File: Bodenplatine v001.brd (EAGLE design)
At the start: 160 x 100 mm, 0 parts

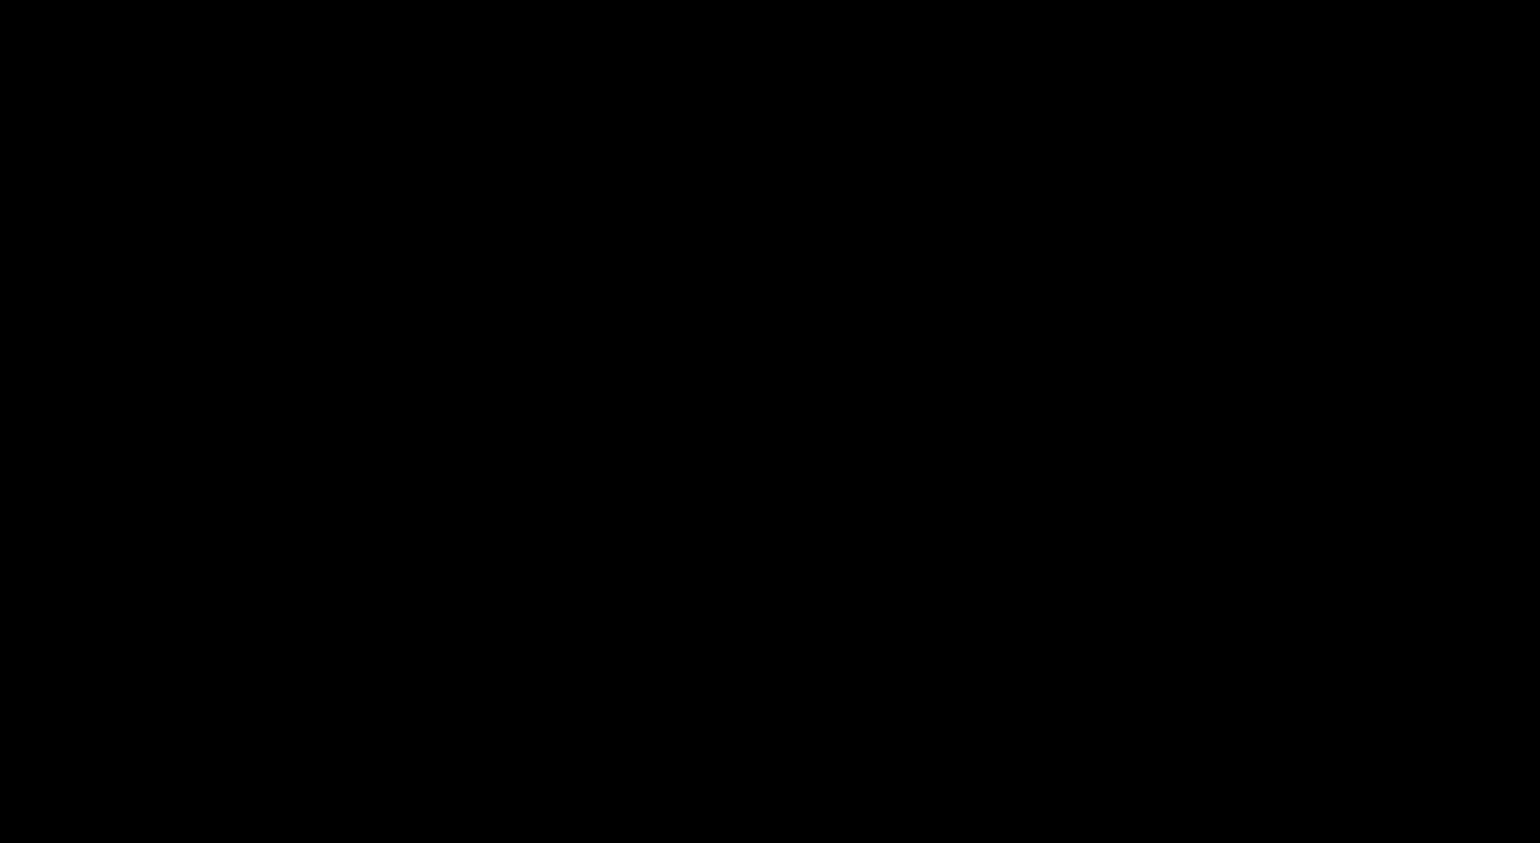
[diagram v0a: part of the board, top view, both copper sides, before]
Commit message: Erste Version der Projekt eigenen Eagle Library
Alle Parts sollen von nun an für jedes Projekt in eine seperate Eagle lbr Datei gepackt werden. Nur Teile aus dieser Library sollen verwendet werden.

Das geschieht um einen besseren Überblick über die verwendeten Teile zu erhalten. Außerdem kann die Eagle Zeichnung incl. der Parts weiter gegeben werden.
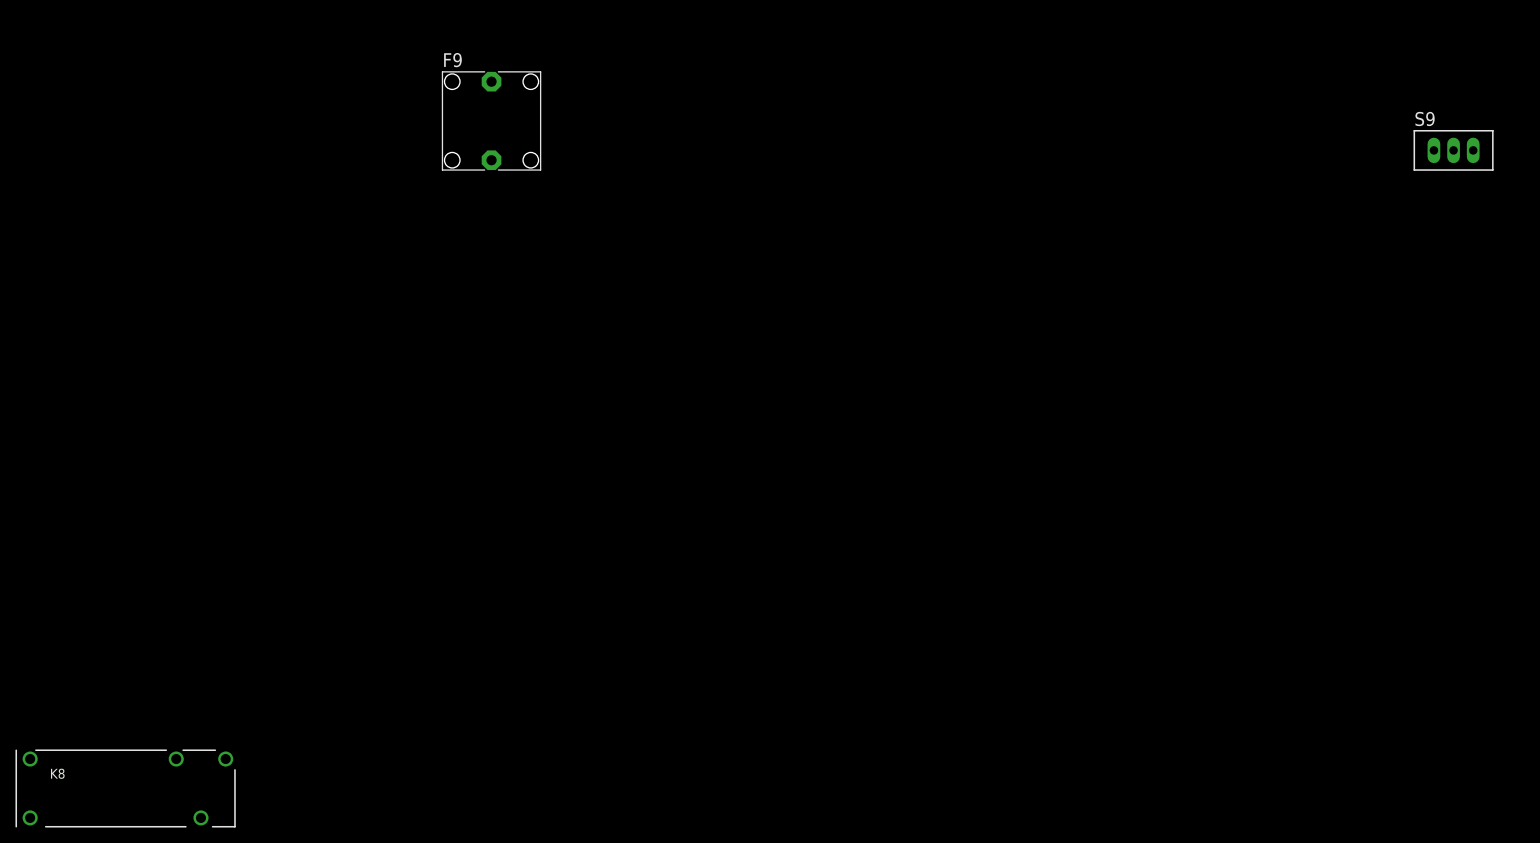
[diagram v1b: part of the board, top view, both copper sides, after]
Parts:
- added F9: (no value), xMZ-Mod-Touch-Bodenplatine:F456
- added K8: RY210005, xMZ-Mod-Touch-Bodenplatine:RY-II
- added S9: TL39PO, xMZ-Mod-Touch-Bodenplatine:TL3XPO
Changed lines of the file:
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@@
 </autorouter>
 <elements>
+<element name="S9" library="xMZ-Mod-Touch-Bodenplatine" package="TL3XPO" value="TL39PO" x="-97.79" y="6.35"/>
+<element name="F9" library="xMZ-Mod-Touch-Bodenplatine" package="F456" value="" x="-222.25" y="10.16">
+<attribute name="OC_NEWARK" value="unknown" x="-222.25" y="10.16" size="1.778" layer="27" font="vector" ratio="15" display="off"/>
+<attribute name="MPN" value="" x="-222.25" y="10.16" size="1.778" layer="27" font="vector" ratio="15" display="off"/>
+<attribute name="MF" value="" x="-222.25" y="10.16" size="1.778" layer="27" font="vector" ratio="15" display="off"/>
+<attribute name="OC_FARNELL" value="unknown" x="-222.25" y="10.16" size="1.778" layer="27" font="vector" ratio="15" display="off"/>
+</element>
+<element name="K8" library="xMZ-Mod-Touch-Bodenplatine" package="RY-II" value="RY210005" x="-269.24" y="-76.2">
+<attribute name="OC_NEWARK" value="08H3762" x="-269.24" y="-76.2" size="1.778" layer="27" font="vector" ratio="15" display="off"/>
+<attribute name="MPN" value="RY210005" x="-269.24" y="-76.2" size="1.778" layer="27" font="vector" ratio="15" display="off"/>
+<attribute name="MF" value="TYCO ELECTRONICS" x="-269.24" y="-76.2" size="1.778" layer="27" font="vector" ratio="15" display="off"/>
+<attribute name="OC_FARNELL" value="unknown" x="-269.24" y="-76.2" size="1.778" layer="27" font="vector" ratio="15" display="off"/>
+</element>
 </elements>
 <signals>

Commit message: Erste fast fertige Version des Schaltplans der Bodebplatine
Es fehlt nur noch die Wago Klemme für L/N/PE Netzteil und 12V+/-
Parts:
- removed S9: TL39PO, xMZ-Mod-Touch-Bodenplatine:TL3XPO
- added D1, D13, D14, D15, D16, D2, D25, D3, D4: BAT54, diode:SOT23
- added D10, D11, D12, D21, D22, D23, D24, D27, D9: 1N4148W, diode:DO35-7
- added D17, D18, D19, D20, D26, D5, D6, D7, D8: Yellow, SparkFun-LED:LED-0603
- added F1, F10, F11, F12, F2, F3, F4, F5, F6, F7, F8: (no value), xMZ-Mod-Touch-Bodenplatine:F456
- added JP1: (no value), pinhead:2X10
- added K1, K2, K3, K4, K5, K6, K7, K9: RY612012, xMZ-Mod-Touch-Bodenplatine:RY-II
- added Q1, Q2, Q3, Q4, Q5, Q6, Q7, Q8, Q9: BC846, AWJLEagleLib:SOT-363
- added R1, R13, R14, R15, R16, R2, R25, R3, R4: 270R, rcl:M0805
- added R10, R11, R12, R21, R22, R23, R24, R27, R9: 10k, rcl:R0603
- added R17, R18, R19, R20, R26, R5, R6, R7, R8: 2k2, rcl:R0603
- added X1, X13, X2, X3, X4, X5, X6, X7, X8, X9: SPRINGCON_AST125_5X2, xMZ-Mod-Touch-Bodenplatine:SPRINGCON_AST125_5X2
- added X10: SPRINGCON_AST125_3X2, xMZ-Mod-Touch-Bodenplatine:SPRINGCON_AST125_3X2
- added X11, X12: SPRINGCON_AST125_4X2, xMZ-Mod-Touch-Bodenplatine:SPRINGCON_AST125_4X2
- K8: value RY210005 -> RY612012
- moved K8 765.8 mm to (-882.6, -534.7)
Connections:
- new net 12V: F10.1, F11.1, JP1.12
- new net 5V: JP1.10, JP1.9
- new net A-: JP1.20, X13.4, X13.4'
- new net AKKU: JP1.16
- new net B+: JP1.19, X13.3
- new net GND: D17.C, D18.C, D19.C, D20.C, D26.C, D5.C, D6.C, D7.C, D8.C, JP1.7, JP1.8, Q1.1, Q2.1, Q3.1, Q4.1, Q5.1, Q6.1, Q7.1, Q8.1, Q9.1, X13.2
- new net L: F9.1
- new net N: X1.4, X2.4, X3.4, X4.4, X5.4, X6.4, X7.4, X8.4, X9.4
- new net N$1: F1.1, X1.2
- new net N$10: Q1.2, R9.2
- new net N$108: JP1.17
- new net N$11: D9.C, K1.A2
- new net N$12: F2.2, K2.11
- new net N$13: D2.1, R2.1
- new net N$14: D2.3, R10.1, R6.2
- new net N$15: D6.A, R6.1
- new net N$16: Q2.2, R10.2
- new net N$17: D10.C, K2.A2
- new net N$18: D10.A, K2.A1, Q2.6
- new net N$19: F2.1, X2.2
- new net N$2: K1.14, X1.3
- new net N$20: K2.12, X2.1
- new net N$21: K3.14, X3.3
- new net N$22: F3.2, K3.11
- new net N$23: D3.1, R3.1
- new net N$24: D3.3, R11.1, R7.2
- new net N$25: D7.A, R7.1
- new net N$26: Q3.2, R11.2
- new net N$27: D11.C, K3.A2
- new net N$28: D11.A, K3.A1, Q3.6
- new net N$29: F3.1, X3.2
- new net N$3: F1.2, K1.11
- new net N$30: K3.12, X3.1
- new net N$31: K4.14, X4.3
- new net N$32: F4.2, K4.11
- new net N$33: D4.1, R4.1
- new net N$34: D4.3, R12.1, R8.2
- new net N$35: D8.A, R8.1
- new net N$36: Q4.2, R12.2
- new net N$37: D12.C, K4.A2
- new net N$38: D12.A, K4.A1, Q4.6
- new net N$39: F4.1, X4.2
- new net N$4: K1.12, X1.1
- new net N$40: K4.12, X4.1
- new net N$41: K5.14, X5.3
- new net N$42: F5.2, K5.11
- new net N$43: D13.1, R13.1
- new net N$44: D13.3, R17.2, R21.1
- new net N$45: D17.A, R17.1
- new net N$46: Q5.2, R21.2
- new net N$47: D21.C, K5.A2
- new net N$48: D21.A, K5.A1, Q5.6
- new net N$49: F5.1, X5.2
- new net N$5: D9.A, K1.A1, Q1.6
- new net N$50: K5.12, X5.1
- new net N$51: K6.14, X6.3
- new net N$52: F6.2, K6.11
- new net N$53: D14.1, R14.1
- new net N$54: D14.3, R18.2, R22.1
- new net N$55: D18.A, R18.1
- new net N$56: Q6.2, R22.2
- new net N$57: D22.C, K6.A2
- new net N$58: D22.A, K6.A1, Q6.6
- new net N$59: F6.1, X6.2
- new net N$6: K2.14, X2.3
- new net N$60: K6.12, X6.1
- new net N$61: K7.14, X7.3
- new net N$62: F7.2, K7.11
- new net N$63: D15.1, R15.1
- new net N$64: D15.3, R19.2, R23.1
- new net N$65: D19.A, R19.1
- new net N$66: Q7.2, R23.2
- new net N$67: D23.C, K7.A2
- new net N$68: D23.A, K7.A1, Q7.6
- new net N$69: F7.1, X7.2
- new net N$7: D1.1, R1.1
- new net N$70: K7.12, X7.1
- new net N$71: K8.14, X8.3
- new net N$72: F8.2, K8.11
- new net N$73: D16.1, R16.1
- new net N$74: D16.3, R20.2, R24.1
- new net N$75: D20.A, R20.1
- new net N$76: Q8.2, R24.2
- new net N$77: D24.C, K8.A2
- new net N$78: D24.A, K8.A1, Q8.6
- new net N$79: F8.1, X8.2
- new net N$8: D1.3, R5.2, R9.1
- new net N$80: K8.12, X8.1
- new net N$81: K9.14, X9.3
- new net N$82: F12.2, K9.11
- new net N$83: D25.1, R25.1
- new net N$84: D25.3, R26.2, R27.1
- new net N$85: D26.A, R26.1
- new net N$86: Q9.2, R27.2
- new net N$87: D27.C, K9.A2
- new net N$88: D27.A, K9.A1, Q9.6
- new net N$89: F12.1, X9.2
- new net N$9: D5.A, R5.1
- new net N$90: K9.12, X9.1
- new net N$91: F9.2
- new net N$92: F11.2, X13.1
- new net N$94: F10.2
- new net N$98: JP1.18
- new net P1: JP1.6, R25.2
- new net P2: JP1.4, R1.2
- new net P3: JP1.2, R2.2
- new net P4: JP1.1, R3.2
- new net P5: JP1.3, R4.2
- new net P6: JP1.5, R13.2
- new net P7: JP1.11, R14.2
- new net P8: JP1.13, R15.2
- new net P9: JP1.15, R16.2
- new net PE: X1.5, X1.5', X2.5, X2.5', X3.5, X3.5', X4.5, X4.5', X5.5, X5.5', X6.5, X6.5', X7.5, X7.5', X8.5, X8.5', X9.5, X9.5'
- new net SCHIRM: X13.5
- new net UB: JP1.14

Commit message: Begin mit dem Bord der Bodenplatine
Schriften in den Schaltplänen einheitlich gemacht (Layer und Große)
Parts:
- added H1, H2, H3, H4: MOUNT-HOLE3.3, holes:3,3
- added X14: 236-403, con-wago_236:P-236-403
- added X15: 236-402, con-wago_236:P-236-402
- F1, F11, F12, F2, F3, F4, F5, F6, F7, F8: value (none) -> 3,15AT
- F10: value (none) -> 6,3AT
- F9: value (none) -> 10AT
- JP1: value (none) -> Stiftleiste 2x20 pol
- moved X13 1066.3 mm to (25.7, -194.4)
- moved X2 980.6 mm to (-53.9, 124.8)
- moved X12 963.8 mm to (-24.4, -248.5)
- moved X8 933.2 mm to (-60.1, -122.2)
- moved X3 932.9 mm to (-72.9, 9.06)
- moved X5 923.0 mm to (-82.8, -70.7)
- moved X11 871.3 mm to (-22.4, -35.1)
- moved X9 867.5 mm to (-184.9, -103.3)
- moved X4 847.1 mm to (-130.4, -19.2)
- moved X6 846.1 mm to (-128.4, -103.2)
- moved X7 836.3 mm to (-86.3, -169.2)
- moved D1 712.1 mm to (-293.8, 41.6)
- moved D10 712.1 mm to (-286.1, -37.1)
- moved D11 712.1 mm to (-286.1, -112.1)
- moved D12 712.1 mm to (-273.4, -112.1)
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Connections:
- removed net AKKU: JP1.16
- removed net N$108: JP1.17
- removed net N$98: JP1.18
- removed net UB: JP1.14
- net 12V: now also X15.L1.1, X15.L1.2
- net GND: now also X12.3, X12.4, X15.L2.1, X15.L2.2
- net L: now also X11.1, X11.2, X11.3, X11.4, X14.L1.1, X14.L1.2
- net N: now also X10.2, X14.L2.1, X14.L2.2
- net N$1: now also X2.2; no longer X1.2
- net N$19: now also X3.2; no longer X2.2
- net N$2: now also X2.3; no longer X1.3
- net N$20: now also X3.1; no longer X2.1
- net N$21: now also X4.3; no longer X3.3
- net N$29: now also X4.2; no longer X3.2
- net N$30: now also X4.1; no longer X3.1
- net N$31: now also X5.3; no longer X4.3
- net N$39: now also X5.2; no longer X4.2
- net N$4: now also X2.1; no longer X1.1
- net N$40: now also X5.1; no longer X4.1
- net N$41: now also X6.3; no longer X5.3
- net N$49: now also X6.2; no longer X5.2
- net N$50: now also X6.1; no longer X5.1
- net N$51: now also X7.3; no longer X6.3
- net N$59: now also X7.2; no longer X6.2
- net N$6: now also X3.3; no longer X2.3
- net N$60: now also X7.1; no longer X6.1
- net N$61: now also X8.3; no longer X7.3
- net N$69: now also X8.2; no longer X7.2
- net N$70: now also X8.1; no longer X7.1
- net N$71: now also X9.3; no longer X8.3
- net N$79: now also X9.2; no longer X8.2
- net N$80: now also X9.1; no longer X8.1
- net N$81: now also X1.3; no longer X9.3
- net N$89: now also X1.2; no longer X9.2
- net N$90: now also X1.1; no longer X9.1
- net N$91: now also X10.1
- net N$94: now also X12.1, X12.2
- net PE: now also X10.3, X14.L3.1, X14.L3.2
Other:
- board size 160 x 100 mm -> 290 x 145 mm

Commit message: Relais neu sortiert (umbenannt)
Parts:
- moved K9 625.4 mm to (230.8, 98.2), turned to 270 degrees
- moved X15 593.3 mm to (41.8, 132.3), turned to 90 degrees
- moved X14 559.1 mm to (14.7, 131.9), turned to 90 degrees
- moved K8 550.5 mm to (208.8, 98.4), turned to 270 degrees
- moved K7 550.5 mm to (180.3, 97.2), turned to 270 degrees
- moved K6 485.6 mm to (154.3, 100.4), turned to 270 degrees
- moved K5 485.0 mm to (125.8, 98.4), turned to 270 degrees
- moved X9 456.1 mm to (239.1, 64.7)
- moved K4 430.7 mm to (95.5, 98.9), turned to 270 degrees
- moved JP1 425.8 mm to (141.9, 130.0)
- moved K3 407.6 mm to (74.2, 99.9), turned to 270 degrees
- moved X7 355.4 mm to (180.7, 65.3)
- moved K2 354.1 mm to (45.6, 98.9), turned to 270 degrees
- moved X12 341.7 mm to (181.1, 24.5)
- moved X8 329.0 mm to (209.9, 65.8)
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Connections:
- net N$11: now also K2.A2; no longer K1.A2
- net N$12: now also K3.11; no longer K2.11
- net N$17: now also K3.A2; no longer K2.A2
- net N$18: now also K3.A1; no longer K2.A1
- net N$2: now also K2.14; no longer K1.14
- net N$20: now also K3.12; no longer K2.12
- net N$21: now also K4.14; no longer K3.14
- net N$22: now also K4.11; no longer K3.11
- net N$27: now also K4.A2; no longer K3.A2
- net N$28: now also K4.A1; no longer K3.A1
- net N$3: now also K2.11; no longer K1.11
- net N$30: now also K4.12; no longer K3.12
- net N$31: now also K5.14; no longer K4.14
- net N$32: now also K5.11; no longer K4.11
- net N$37: now also K5.A2; no longer K4.A2
- net N$38: now also K5.A1; no longer K4.A1
- net N$4: now also K2.12; no longer K1.12
- net N$40: now also K5.12; no longer K4.12
- net N$41: now also K6.14; no longer K5.14
- net N$42: now also K6.11; no longer K5.11
- net N$47: now also K6.A2; no longer K5.A2
- net N$48: now also K6.A1; no longer K5.A1
- net N$5: now also K2.A1; no longer K1.A1
- net N$50: now also K6.12; no longer K5.12
- net N$51: now also K7.14; no longer K6.14
- net N$52: now also K7.11; no longer K6.11
- net N$57: now also K7.A2; no longer K6.A2
- net N$58: now also K7.A1; no longer K6.A1
- net N$6: now also K3.14; no longer K2.14
- net N$60: now also K7.12; no longer K6.12
- net N$61: now also K8.14; no longer K7.14
- net N$62: now also K8.11; no longer K7.11
- net N$67: now also K8.A2; no longer K7.A2
- net N$68: now also K8.A1; no longer K7.A1
- net N$70: now also K8.12; no longer K7.12
- net N$71: now also K9.14; no longer K8.14
- net N$72: now also K9.11; no longer K8.11
- net N$77: now also K9.A2; no longer K8.A2
- net N$78: now also K9.A1; no longer K8.A1
- net N$80: now also K9.12; no longer K8.12
- net N$81: now also K1.14; no longer K9.14
- net N$82: now also K1.11; no longer K9.11
- net N$87: now also K1.A2; no longer K9.A2
- net N$88: now also K1.A1; no longer K9.A1
- net N$90: now also K1.12; no longer K9.12

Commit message: Tiny Switches über den Relais vergessen
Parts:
- removed F11: 3,15AT, xMZ-Mod-Touch-Bodenplatine:F456
- added F13: 3,15AT, xMZ-Mod-Touch-Bodenplatine:F456
- added S1, S2, S3, S4, S5, S6, S7, S8, S9: TL39PO, xMZ-Mod-Touch-Bodenplatine:TL3XPO
- F10: value 6,3AT -> 10AT
- F12: value 3,15AT -> 6,3AT
- F9: value 10AT -> 3,15AT
- moved H3 799.9 mm to (278.8, 130.7)
- moved H2 732.4 mm to (274.8, 11.1)
- moved H4 590.4 mm to (7.31, 116.8)
- moved F8 586.1 mm to (225.6, 89.7)
- moved F10 509.9 mm to (96.8, 28.2)
- moved F7 500.5 mm to (197.1, 85.2)
- moved F12 499.7 mm to (152.8, 36.2)
- moved H1 495.4 mm to (6.31, 6.00)
- moved F6 486.3 mm to (167.2, 84.7)
- moved D13 473.2 mm to (16.9, 203.4)
- moved D14 473.2 mm to (24.5, 203.4)
- moved D15 473.2 mm to (-41.6, 191.9)
- moved D16 473.2 mm to (-33.9, 191.9)
- moved D17 473.2 mm to (-26.3, 179.2)
- moved D18 473.2 mm to (-22.5, 179.2)
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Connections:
- net 12V: now also F12.1, F13.1; no longer F10.1, F11.1
- net 5V: now also S1.3, S2.3, S3.3, S4.3, S5.3, S6.3, S7.3, S8.3, S9.3
- net GND: now also S1.1, S2.1, S3.1, S4.1, S5.1, S6.1, S7.1, S8.1, S9.1
- net L: now also F10.1; no longer F9.1
- net N$1: now also F2.1; no longer F1.1
- net N$12: now also F3.2; no longer F2.2
- net N$14: now also S3.2
- net N$19: now also F3.1; no longer F2.1
- net N$22: now also F4.2; no longer F3.2
- net N$24: now also S4.2
- net N$29: now also F4.1; no longer F3.1
- net N$3: now also F2.2; no longer F1.2
- net N$32: now also F5.2; no longer F4.2
- net N$34: now also S5.2
- net N$39: now also F5.1; no longer F4.1
- net N$42: now also F6.2; no longer F5.2
- net N$44: now also S6.2
- net N$49: now also F6.1; no longer F5.1
- net N$52: now also F7.2; no longer F6.2
- net N$54: now also S7.2
- net N$59: now also F7.1; no longer F6.1
- net N$62: now also F8.2; no longer F7.2
- net N$64: now also S8.2
- net N$69: now also F8.1; no longer F7.1
- net N$72: now also F9.2; no longer F8.2
- net N$74: now also S9.2
- net N$79: now also F9.1; no longer F8.1
- net N$8: now also S2.2
- net N$82: now also F1.2; no longer F12.2
- net N$84: now also S1.2
- net N$89: now also F1.1; no longer F12.1
- net N$91: now also F10.2; no longer F9.2
- net N$92: now also F13.2; no longer F11.2
- net N$94: now also F12.2; no longer F10.2

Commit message: BC486 ausgetauscht
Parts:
- Q1, Q2, Q3, Q4, Q5, Q6, Q7, Q8: value BC846 -> BC846BLT1SMD; device AWJLEagleLib:SOT-363 -> xMZ-Mod-Touch-Bodenplatine:SOT23
- moved S9 1516.6 mm to (269.0, 121.5)
- moved S8 1480.4 mm to (240.0, 119.5)
- moved S7 1443.7 mm to (209.5, 118.5)
- moved S6 1410.2 mm to (182.5, 117.5)
- moved S5 1373.5 mm to (151.0, 117.0)
- moved S4 1338.1 mm to (121.0, 116.0)
- moved S3 1305.6 mm to (91.0, 119.5)
- moved S2 1272.6 mm to (62.5, 119.0)
- moved S1 1237.9 mm to (31.5, 118.5)
- moved D24 308.2 mm to (275.6, 116.2), turned to 180 degrees
- moved D23 284.2 mm to (237.8, 114.7), turned to 180 degrees
- moved Q8 262.7 mm to (-90.0, -56.5)
- moved Q1 261.2 mm to (-90.0, -4.00)
- moved Q7 253.1 mm to (-90.0, -49.0)
- moved Q2 246.2 mm to (-90.0, -11.5)
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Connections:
- net GND: now also Q1.2, Q2.2, Q3.2, Q4.2, Q5.2, Q6.2, Q7.2, Q8.2; no longer Q1.1, Q2.1, Q3.1, Q4.1, Q5.1, Q6.1, Q7.1, Q8.1
- net N$10: now also Q1.1; no longer Q1.2
- net N$16: now also Q2.1; no longer Q2.2
- net N$18: now also Q2.3; no longer Q2.6
- net N$26: now also Q3.1; no longer Q3.2
- net N$28: now also Q3.3; no longer Q3.6
- net N$36: now also Q4.1; no longer Q4.2
- net N$38: now also Q4.3; no longer Q4.6
- net N$46: now also Q5.1; no longer Q5.2
- net N$48: now also Q5.3; no longer Q5.6
- net N$5: now also Q1.3; no longer Q1.6
- net N$56: now also Q6.1; no longer Q6.2
- net N$58: now also Q6.3; no longer Q6.6
- net N$66: now also Q7.1; no longer Q7.2
- net N$68: now also Q7.3; no longer Q7.6
- net N$76: now also Q8.1; no longer Q8.2
- net N$78: now also Q8.3; no longer Q8.6

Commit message: Korrektur zum letzten Commit, Ein BC486 vergessen
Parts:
- Q9: value BC846 -> BC846BLT1SMD; device AWJLEagleLib:SOT-363 -> xMZ-Mod-Touch-Bodenplatine:SOT23
- moved Q8 360.5 mm to (230.5, 108.5)
- moved Q7 331.2 mm to (203.0, 105.5)
- moved Q9 307.9 mm to (265.5, 110.5)
- moved Q6 303.5 mm to (175.0, 106.5)
- moved Q5 271.3 mm to (143.0, 105.0)
- moved Q4 242.0 mm to (112.5, 106.0)
- moved Q3 212.4 mm to (82.5, 105.0)
- moved Q2 186.2 mm to (54.5, 106.0)
- moved Q1 156.6 mm to (21.5, 106.0)
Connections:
- net GND: now also Q9.2; no longer Q9.1
- net N$10: now also Q2.1; no longer Q1.1
- net N$16: now also Q3.1; no longer Q2.1
- net N$18: now also Q3.3; no longer Q2.3
- net N$26: now also Q4.1; no longer Q3.1
- net N$28: now also Q4.3; no longer Q3.3
- net N$36: now also Q5.1; no longer Q4.1
- net N$38: now also Q5.3; no longer Q4.3
- net N$46: now also Q6.1; no longer Q5.1
- net N$48: now also Q6.3; no longer Q5.3
- net N$5: now also Q2.3; no longer Q1.3
- net N$56: now also Q7.1; no longer Q6.1
- net N$58: now also Q7.3; no longer Q6.3
- net N$66: now also Q8.1; no longer Q7.1
- net N$68: now also Q8.3; no longer Q7.3
- net N$76: now also Q9.1; no longer Q8.1
- net N$78: now also Q9.3; no longer Q8.3
- net N$86: now also Q1.1; no longer Q9.2
- net N$88: now also Q1.3; no longer Q9.6
